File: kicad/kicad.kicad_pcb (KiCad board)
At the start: 2 copper layers, 100 x 100 mm, 109 parts, among them J101 DEBUG_LED_CONN, J102 EPD_SPI_CONN, J103 HPC_CONN, J104 STORAGE_CONN, J105 USBC_CONN, J106 GLOBAL_CONN, J107 INPUT_CONN, J108 CHARGER_CONN, J201 USB_C_Receptacle_USB2.0_16P, J301 BATTERY_CONN, J501 MOTOR_P_SF, J502 MOTOR_N_SF, Q301 2N7002, Q401 SI1308EDL, SW701 PLACEHOLDER_BT1, SW702 PLACEHOLDER_BT2, SW703 PLACEHOLDER_BT3, SW704 BT1, SW705 BT2, SW706 BT3, SW707 BT4, U201 TPD2S300, U301 BQ21061, U501 DA7280, U601 M95P32

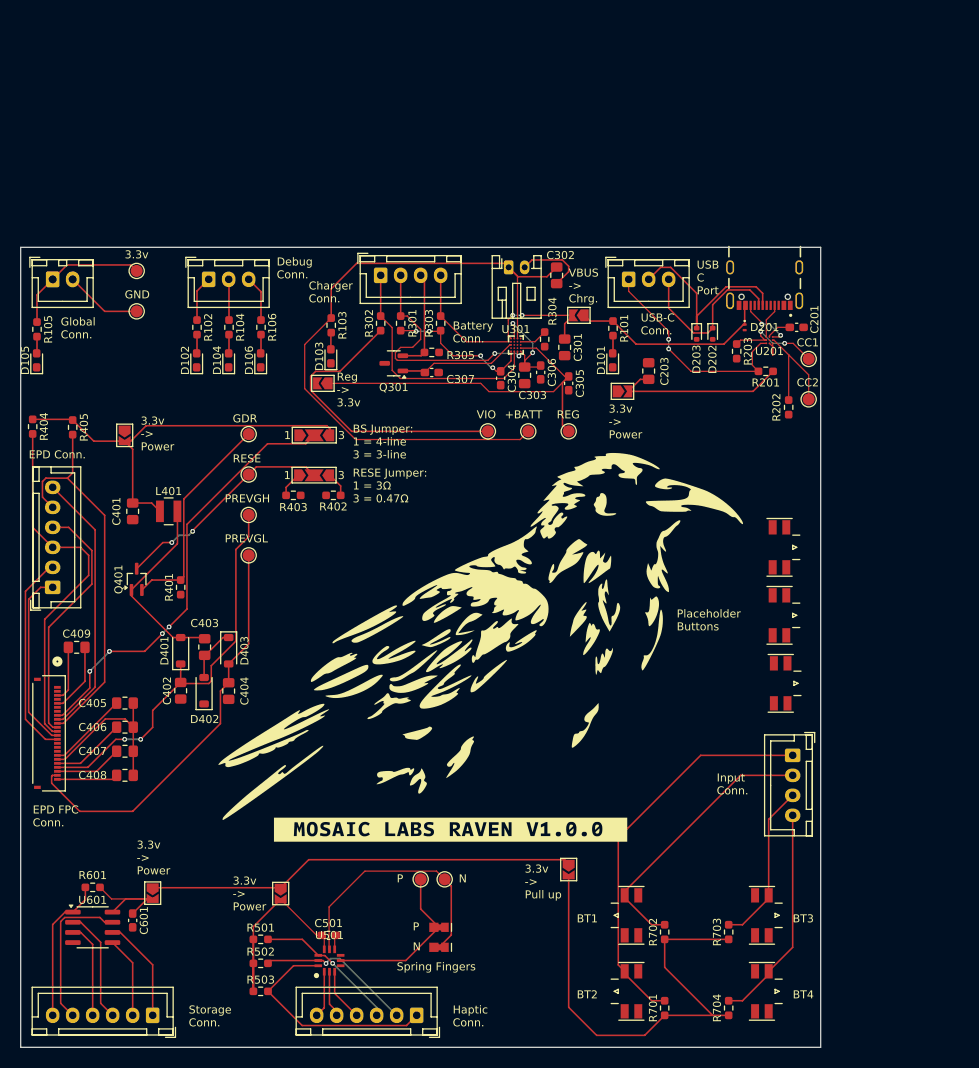
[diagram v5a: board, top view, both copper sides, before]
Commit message: refactor usb-c module, remove unnecessary ICs
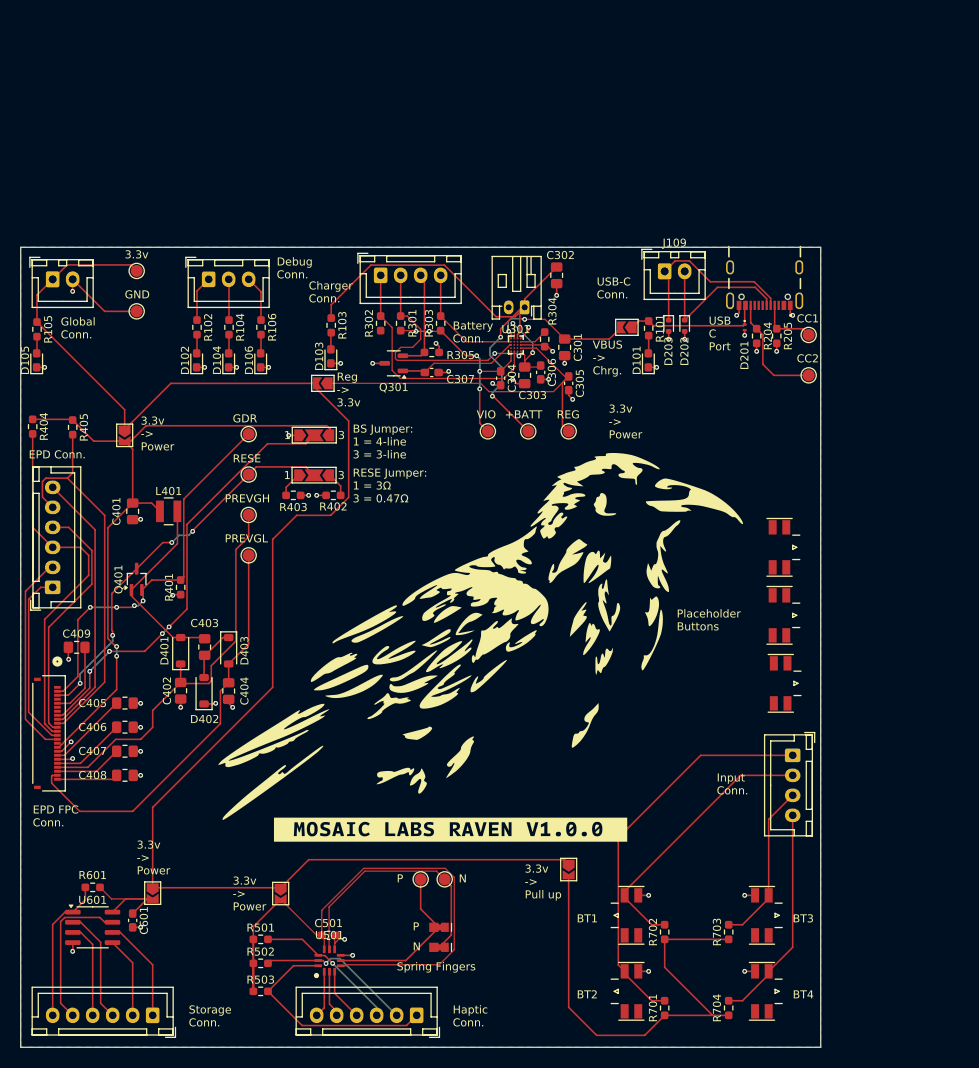
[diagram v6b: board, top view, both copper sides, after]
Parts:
- removed C201: 100nF, Capacitor_SMD:C_0603_1608Metric_Pad1.08x0.95mm_HandSolder
- removed C203: 1uF, Capacitor_SMD:C_0805_2012Metric_Pad1.18x1.45mm_HandSolder
- removed J105: USBC_CONN, Connector_JST:JST_XH_B3B-XH-A_1x03_P2.50mm_Vertical
- removed JP104: USB_PWR_JP, Jumper:SolderJumper-2_P1.3mm_Open_TrianglePad1.0x1.5mm
- removed R201: 10k, Resistor_SMD:R_0603_1608Metric_Pad0.98x0.95mm_HandSolder
- removed R202, R203: 5.1k, Resistor_SMD:R_0603_1608Metric_Pad0.98x0.95mm_HandSolder
- removed U201: TPD2S300, Raven:YFF0009AJAJ
- added J109: USBC_CONN, Connector_JST:JST_XH_B2B-XH-A_1x02_P2.50mm_Vertical, F.Cu at (173.5, 50.0)
- added R204: 5.1k, Resistor_SMD:R_0603_1608Metric_Pad0.98x0.95mm_HandSolder, F.Cu at (185.0, 58.1)
- added R205: 5.1k, Resistor_SMD:R_0603_1608Metric_Pad0.98x0.95mm_HandSolder, F.Cu at (187.5, 58.1)
- moved JP106 6.18 mm to (168.8, 57.0)
- moved J301 5.39 mm to (156.0, 54.5), turned to 180 degrees
- moved D101 4.46 mm to (171.5, 61.1)
- moved R101 4.46 mm to (171.5, 57.1)
- moved D202 3.64 mm to (176.0, 56.8)
- moved D203 3.64 mm to (174.0, 56.8)
- moved TP201 3.00 mm to (191.5, 58.0)
- moved TP202 3.00 mm to (191.5, 63.0)
- renumbered 3.3v to TP101, GND to TP102, OUTP_TP to TP501, OUTN_TP to TP502
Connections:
- J201 pad A5: Net-(J201-CC1) -> /USB-C/CC1_T
- J201 pad B5: Net-(J201-CC2) -> /USB-C/CC2_T
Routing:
- net +3.3V: track 71.4 -> 193.1 mm
- net /Haptics/PWR: track 31.8 -> 78.2 mm
- net /E-Paper Display/PWR: track 52.1 -> 87.6 mm, vias 0 -> 2
- net /Battery Management V2/VIO: track 55.9 -> 26.6 mm, vias 4 -> 5
- net /USB-C/FLT_N: track 28.1 -> 0.00 mm, vias 2 -> 0
- net /USB-C/IC_PWR: track 25.5 -> 0.00 mm
- net GND: track 48.5 -> 73.3 mm, vias 0 -> 48
- net +BATT: track 84.9 -> 62.5 mm, vias 0 -> 2
- net /E-Paper Display/GDR: track 27.1 -> 48.1 mm, vias 0 -> 4
- net /E-Paper Display/RESE: track 27.9 -> 48.7 mm, vias 2 -> 4
- net VBUS: track 24.9 -> 17.1 mm
- net Net-(J201-CC2): track 6.95 -> 0.00 mm, vias 2 -> 0
- net /USB-C/CC1_T: track 12.8 -> 7.34 mm, vias 2 -> 0
- net Net-(J201-CC1): track 4.38 -> 0.00 mm
- net /Battery Management V2/CHRG: track 14.2 -> 18.2 mm
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- added copper zone on B.Cu, net GND

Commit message: finish pcb v1.0.0
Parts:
- removed the G*** at (150.4, 106.6)
- added G***: LOGO, LOGO, F.Cu at (168.5, 110.0)
- added G***: LOGO, LOGO, F.Cu at (146.6, 97.4)
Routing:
- net /Battery Management V2/VIO: track 26.6 -> 32.0 mm, vias 5 -> 6
- net /Haptics/OUTN_T: track 31.5 -> 29.8 mm
- net /Haptics/PWR: track 78.2 -> 77.2 mm
- net GND: track 73.3 -> 73.4 mm, vias 48 -> 49

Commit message: minor fixes, generate fab files
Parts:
- moved D201 5.50 mm to (189.0, 56.9)
- moved R101 3.45 mm to (169.0, 59.5), turned to 0 degrees
- moved D101 2.63 mm to (171.5, 58.5)
- moved D202 1.10 mm to (176.0, 55.7)
- moved D203 1.10 mm to (174.0, 55.7)
- moved TP201 1.05 mm to (191.5, 59.0)
- moved R204 1.02 mm to (184.0, 57.9)
- moved TP202 1.00 mm to (191.5, 64.0)
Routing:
- net /USB-C/CC2_T: track 14.3 -> 48.8 mm
- net VBUS: track 17.1 -> 36.0 mm
- net /USB-C/DM: track 22.9 -> 27.2 mm
- net /USB-C/DP: track 19.5 -> 23.2 mm
- net GND: track 73.4 -> 74.5 mm
